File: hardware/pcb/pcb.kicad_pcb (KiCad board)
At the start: 2 copper layers, 5 parts, among them J1 PRT-12639, K1 KEYSW, U1 RP2040_Zero, U2 Nice_Nano_V2

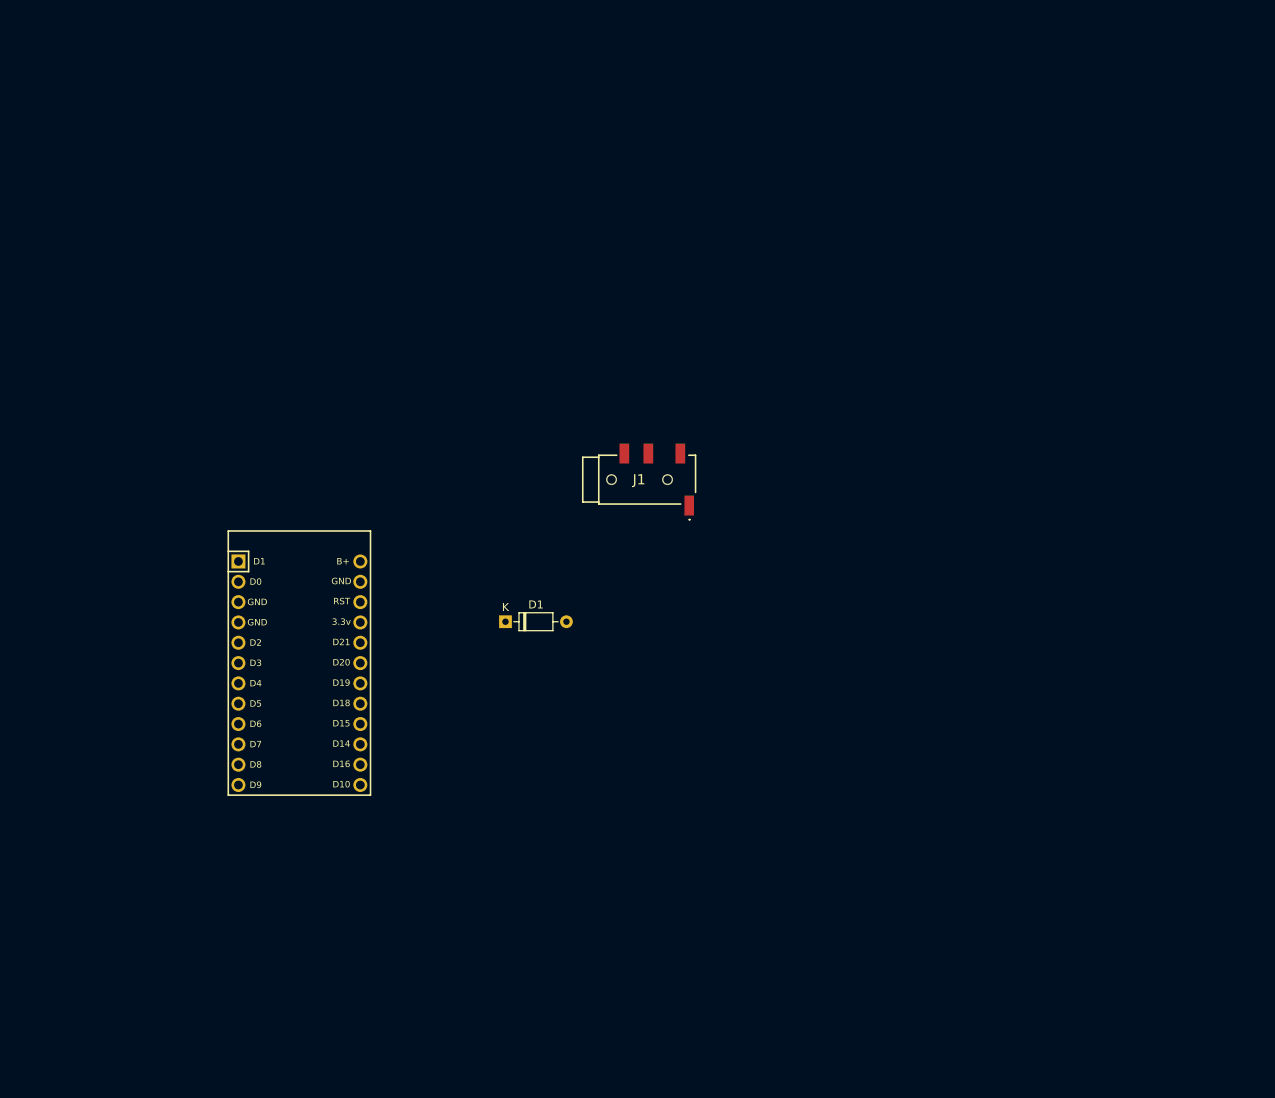
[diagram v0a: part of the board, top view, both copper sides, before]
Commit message: added 6X8 matrix and global labels
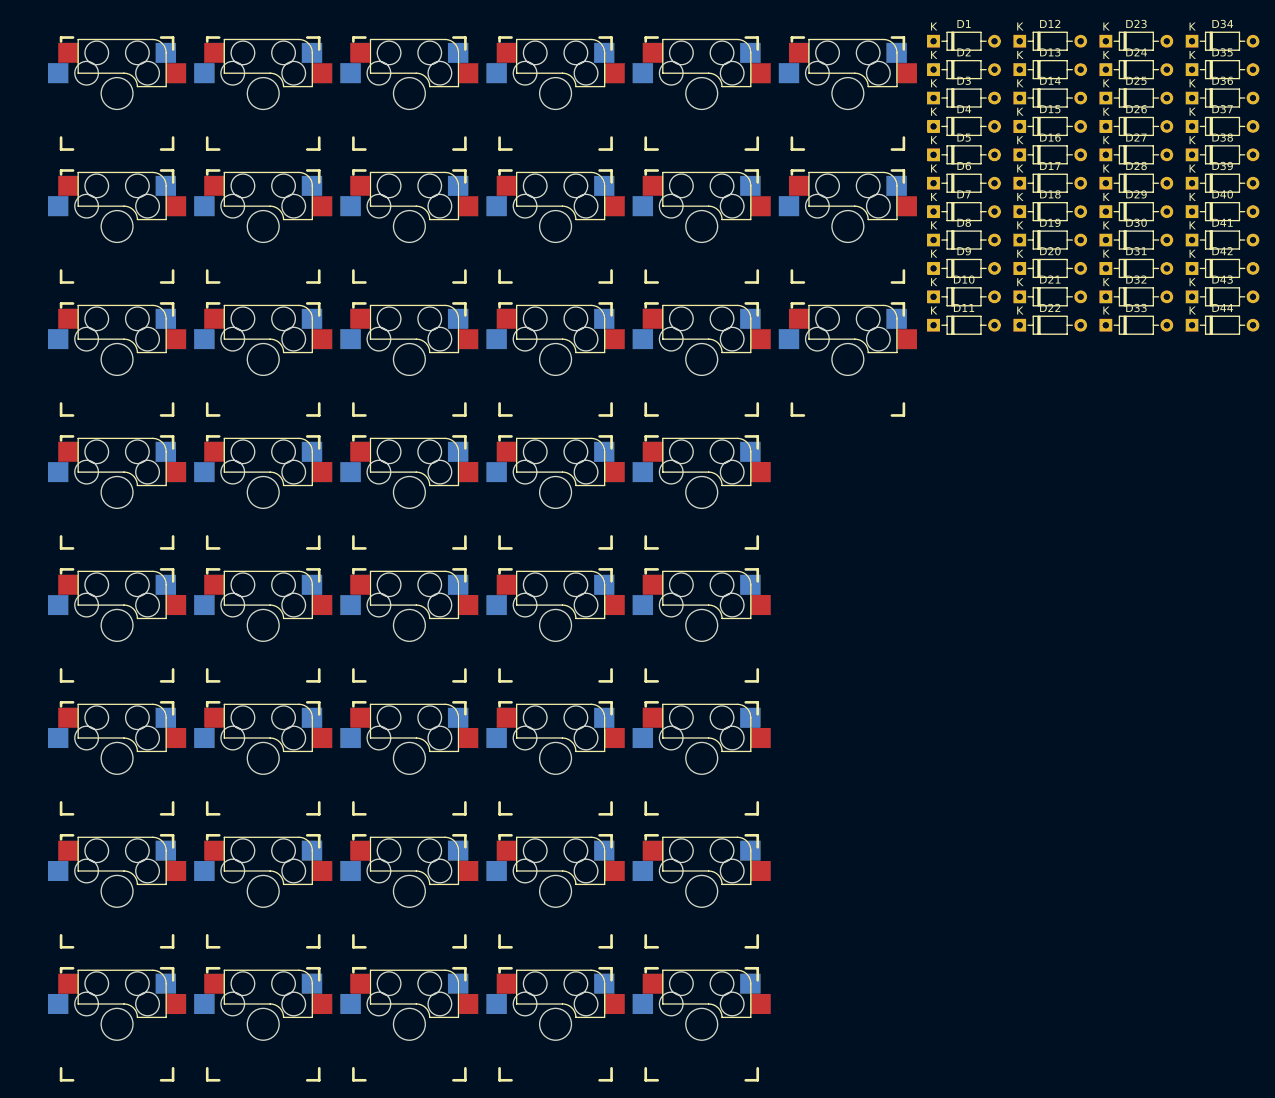
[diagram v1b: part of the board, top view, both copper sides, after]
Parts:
- removed J1: PRT-12639, foot:PRT12639
- removed U2: Nice_Nano_V2, ScottoKeebs_MCU:Nice_Nano_V2
- added D10: Diode, ScottoKeebs_Components:Diode_DO-35, F.Cu at (230.7, 56.4)
- added D11: Diode, ScottoKeebs_Components:Diode_DO-35, F.Cu at (230.7, 59.9)
- added D12: Diode, ScottoKeebs_Components:Diode_DO-35, F.Cu at (241.5, 24.4)
- added D13: Diode, ScottoKeebs_Components:Diode_DO-35, F.Cu at (241.5, 27.9)
- added D14: Diode, ScottoKeebs_Components:Diode_DO-35, F.Cu at (241.5, 31.5)
- added D15: Diode, ScottoKeebs_Components:Diode_DO-35, F.Cu at (241.5, 35.0)
- added D16: Diode, ScottoKeebs_Components:Diode_DO-35, F.Cu at (241.5, 38.6)
- added D17: Diode, ScottoKeebs_Components:Diode_DO-35, F.Cu at (241.5, 42.1)
- added D18: Diode, ScottoKeebs_Components:Diode_DO-35, F.Cu at (241.5, 45.7)
- added D19: Diode, ScottoKeebs_Components:Diode_DO-35, F.Cu at (241.5, 49.2)
- added D2: Diode, ScottoKeebs_Components:Diode_DO-35, F.Cu at (230.7, 27.9)
- added D20: Diode, ScottoKeebs_Components:Diode_DO-35, F.Cu at (241.5, 52.8)
- added D21: Diode, ScottoKeebs_Components:Diode_DO-35, F.Cu at (241.5, 56.4)
- added D22: Diode, ScottoKeebs_Components:Diode_DO-35, F.Cu at (241.5, 59.9)
- added D23: Diode, ScottoKeebs_Components:Diode_DO-35, F.Cu at (252.2, 24.4)
- added D24: Diode, ScottoKeebs_Components:Diode_DO-35, F.Cu at (252.2, 27.9)
- added D25: Diode, ScottoKeebs_Components:Diode_DO-35, F.Cu at (252.2, 31.5)
- added D26: Diode, ScottoKeebs_Components:Diode_DO-35, F.Cu at (252.2, 35.0)
- added D27: Diode, ScottoKeebs_Components:Diode_DO-35, F.Cu at (252.2, 38.6)
- added D28: Diode, ScottoKeebs_Components:Diode_DO-35, F.Cu at (252.2, 42.1)
- added D29: Diode, ScottoKeebs_Components:Diode_DO-35, F.Cu at (252.2, 45.7)
- added D3: Diode, ScottoKeebs_Components:Diode_DO-35, F.Cu at (230.7, 31.5)
- added D30: Diode, ScottoKeebs_Components:Diode_DO-35, F.Cu at (252.2, 49.2)
- added D31: Diode, ScottoKeebs_Components:Diode_DO-35, F.Cu at (252.2, 52.8)
- added D32: Diode, ScottoKeebs_Components:Diode_DO-35, F.Cu at (252.2, 56.4)
- added D33: Diode, ScottoKeebs_Components:Diode_DO-35, F.Cu at (252.2, 59.9)
- added D34: Diode, ScottoKeebs_Components:Diode_DO-35, F.Cu at (263.0, 24.4)
- added D35: Diode, ScottoKeebs_Components:Diode_DO-35, F.Cu at (263.0, 27.9)
- added D36: Diode, ScottoKeebs_Components:Diode_DO-35, F.Cu at (263.0, 31.5)
- added D37: Diode, ScottoKeebs_Components:Diode_DO-35, F.Cu at (263.0, 35.0)
- added D38: Diode, ScottoKeebs_Components:Diode_DO-35, F.Cu at (263.0, 38.6)
- added D39: Diode, ScottoKeebs_Components:Diode_DO-35, F.Cu at (263.0, 42.1)
- added D4: Diode, ScottoKeebs_Components:Diode_DO-35, F.Cu at (230.7, 35.0)
- added D40: Diode, ScottoKeebs_Components:Diode_DO-35, F.Cu at (263.0, 45.7)
- added D41: Diode, ScottoKeebs_Components:Diode_DO-35, F.Cu at (263.0, 49.2)
- added D42: Diode, ScottoKeebs_Components:Diode_DO-35, F.Cu at (263.0, 52.8)
- added D43: Diode, ScottoKeebs_Components:Diode_DO-35, F.Cu at (263.0, 56.4)
- added D44: Diode, ScottoKeebs_Components:Diode_DO-35, F.Cu at (263.0, 59.9)
- added D5: Diode, ScottoKeebs_Components:Diode_DO-35, F.Cu at (230.7, 38.6)
- added D6: Diode, ScottoKeebs_Components:Diode_DO-35, F.Cu at (230.7, 42.1)
- added D7: Diode, ScottoKeebs_Components:Diode_DO-35, F.Cu at (230.7, 45.7)
- added D8: Diode, ScottoKeebs_Components:Diode_DO-35, F.Cu at (230.7, 49.2)
- added D9: Diode, ScottoKeebs_Components:Diode_DO-35, F.Cu at (230.7, 52.8)
- added K10: KEYSW, vbdox:Kailh_MX_Socket_reversible, F.Cu at (146.9, 30.9)
- added K11: KEYSW, vbdox:Kailh_MX_Socket_reversible, F.Cu at (146.9, 47.6)
- added K12: KEYSW, vbdox:Kailh_MX_Socket_reversible, F.Cu at (146.9, 64.2)
- added K13: KEYSW, vbdox:Kailh_MX_Socket_reversible, F.Cu at (146.9, 80.8)
- added K14: KEYSW, vbdox:Kailh_MX_Socket_reversible, F.Cu at (146.9, 97.4)
- added K15: KEYSW, vbdox:Kailh_MX_Socket_reversible, F.Cu at (146.9, 114.0)
- added K16: KEYSW, vbdox:Kailh_MX_Socket_reversible, F.Cu at (146.9, 130.7)
- added K17: KEYSW, vbdox:Kailh_MX_Socket_reversible, F.Cu at (146.9, 147.3)
- added K18: KEYSW, vbdox:Kailh_MX_Socket_reversible, F.Cu at (165.2, 30.9)
- added K19: KEYSW, vbdox:Kailh_MX_Socket_reversible, F.Cu at (165.2, 47.6)
- added K2: KEYSW, vbdox:Kailh_MX_Socket_reversible, F.Cu at (128.6, 30.9)
- added K20: KEYSW, vbdox:Kailh_MX_Socket_reversible, F.Cu at (165.2, 64.2)
- added K21: KEYSW, vbdox:Kailh_MX_Socket_reversible, F.Cu at (165.2, 80.8)
- added K22: KEYSW, vbdox:Kailh_MX_Socket_reversible, F.Cu at (165.2, 97.4)
- added K23: KEYSW, vbdox:Kailh_MX_Socket_reversible, F.Cu at (165.2, 114.0)
- added K24: KEYSW, vbdox:Kailh_MX_Socket_reversible, F.Cu at (165.2, 130.7)
- added K25: KEYSW, vbdox:Kailh_MX_Socket_reversible, F.Cu at (165.2, 147.3)
- added K26: KEYSW, vbdox:Kailh_MX_Socket_reversible, F.Cu at (183.4, 30.9)
- added K27: KEYSW, vbdox:Kailh_MX_Socket_reversible, F.Cu at (183.4, 47.6)
- added K28: KEYSW, vbdox:Kailh_MX_Socket_reversible, F.Cu at (183.4, 64.2)
- added K29: KEYSW, vbdox:Kailh_MX_Socket_reversible, F.Cu at (183.4, 80.8)
- added K3: KEYSW, vbdox:Kailh_MX_Socket_reversible, F.Cu at (128.6, 47.6)
- added K30: KEYSW, vbdox:Kailh_MX_Socket_reversible, F.Cu at (183.4, 97.4)
- added K31: KEYSW, vbdox:Kailh_MX_Socket_reversible, F.Cu at (183.4, 114.0)
- added K32: KEYSW, vbdox:Kailh_MX_Socket_reversible, F.Cu at (183.4, 130.7)
- added K33: KEYSW, vbdox:Kailh_MX_Socket_reversible, F.Cu at (183.4, 147.3)
- added K34: KEYSW, vbdox:Kailh_MX_Socket_reversible, F.Cu at (201.7, 30.9)
- added K35: KEYSW, vbdox:Kailh_MX_Socket_reversible, F.Cu at (201.7, 47.6)
- added K36: KEYSW, vbdox:Kailh_MX_Socket_reversible, F.Cu at (201.7, 64.2)
- added K37: KEYSW, vbdox:Kailh_MX_Socket_reversible, F.Cu at (201.7, 80.8)
- added K38: KEYSW, vbdox:Kailh_MX_Socket_reversible, F.Cu at (201.7, 97.4)
- added K39: KEYSW, vbdox:Kailh_MX_Socket_reversible, F.Cu at (201.7, 114.0)
- added K4: KEYSW, vbdox:Kailh_MX_Socket_reversible, F.Cu at (128.6, 64.2)
- added K40: KEYSW, vbdox:Kailh_MX_Socket_reversible, F.Cu at (201.7, 130.7)
- added K41: KEYSW, vbdox:Kailh_MX_Socket_reversible, F.Cu at (201.7, 147.3)
- added K42: KEYSW, vbdox:Kailh_MX_Socket_reversible, F.Cu at (220.0, 30.9)
- added K43: KEYSW, vbdox:Kailh_MX_Socket_reversible, F.Cu at (220.0, 47.6)
- added K44: KEYSW, vbdox:Kailh_MX_Socket_reversible, F.Cu at (220.0, 64.2)
- added K5: KEYSW, vbdox:Kailh_MX_Socket_reversible, F.Cu at (128.6, 80.8)
- added K6: KEYSW, vbdox:Kailh_MX_Socket_reversible, F.Cu at (128.6, 97.4)
- added K7: KEYSW, vbdox:Kailh_MX_Socket_reversible, F.Cu at (128.6, 114.0)
- added K8: KEYSW, vbdox:Kailh_MX_Socket_reversible, F.Cu at (128.6, 130.7)
- added K9: KEYSW, vbdox:Kailh_MX_Socket_reversible, F.Cu at (128.6, 147.3)
- moved D1 90.2 mm to (230.7, 24.4)
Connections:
- D1 pad 2: unconnected-(D1-A-Pad2) -> Net-(D1-A)
- K1 pad 1: unconnected-(K1-Pad1) -> Net-(D1-A)

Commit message: schema init
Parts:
- added J1: PRT-12639, vbdox:PRT12639, B.Cu at (115.3, 24.9)
- added R1: 2.2K, ScottoKeebs_Components:Diode_DO-35, F.Cu at (95.7, 29.0)
- added R2: 2.2K, ScottoKeebs_Components:Diode_DO-35, F.Cu at (95.7, 34.4)
- D1, D10, D11, D12, D13, D14, D15, D16, D17, D18, D19, D2, D20, D21, D22, D23, D24, D25, D26, D27, D28, D29, D3, D30, D31, D32, D33, D34, D35, D36, D37, D38, D39, D4, D40, D41, D42, D43, D44, D5, D6, D7, D8, D9, U1: moved to B.Cu
- moved D37 211.7 mm to (84.6, 149.1), turned to 90 degrees
- moved D38 193.9 mm to (103.7, 149.1), turned to 90 degrees
- moved D26 188.4 mm to (79.9, 111.1), turned to 90 degrees
- moved D33 186.1 mm to (79.9, 130.2), turned to 90 degrees
- moved D35 182.3 mm to (122.7, 144.4), turned to 90 degrees
- moved D34 168.9 mm to (141.8, 142.0), turned to 90 degrees
- moved D12 168.7 mm to (79.9, 72.9), turned to 90 degrees
- moved D25 168.5 mm to (103.7, 111.0), turned to 90 degrees
- moved D20 166.3 mm to (79.9, 92.1), turned to 90 degrees
- moved D32 165.8 mm to (103.7, 130.1), turned to 90 degrees
- moved D36 152.2 mm to (160.8, 144.4), turned to 90 degrees
- moved D29 152.0 mm to (122.7, 125.3), turned to 90 degrees
- moved D13 144.9 mm to (103.7, 72.9), turned to 90 degrees
- moved D19 144.2 mm to (103.7, 92.0), turned to 90 degrees
- moved K37 138.5 mm to (79.6, 146.1)
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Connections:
- D1 pad 1: unconnected-(D1-K-Pad1) -> C0
- D10 pad 1: unconnected-(D10-K-Pad1) -> C3
- D11 pad 1: unconnected-(D11-K-Pad1) -> C4
- D12 pad 1: unconnected-(D12-K-Pad1) -> C5
- D13 pad 1: unconnected-(D13-K-Pad1) -> C6
- D14 pad 1: unconnected-(D14-K-Pad1) -> C0
- D15 pad 1: unconnected-(D15-K-Pad1) -> C1
- D16 pad 1: unconnected-(D16-K-Pad1) -> C2
- D17 pad 1: unconnected-(D17-K-Pad1) -> C3
- D18 pad 1: unconnected-(D18-K-Pad1) -> C4
- D19 pad 1: unconnected-(D19-K-Pad1) -> C5
- D2 pad 1: unconnected-(D2-K-Pad1) -> C1
- D20 pad 1: unconnected-(D20-K-Pad1) -> C6
- D21 pad 1: unconnected-(D21-K-Pad1) -> C0
- D22 pad 1: unconnected-(D22-K-Pad1) -> C1
- D23 pad 1: unconnected-(D23-K-Pad1) -> C2
- D24 pad 1: unconnected-(D24-K-Pad1) -> C3
- D25 pad 1: unconnected-(D25-K-Pad1) -> C4
- D26 pad 1: unconnected-(D26-K-Pad1) -> C5
- D27 pad 1: unconnected-(D27-K-Pad1) -> C6
- D28 pad 1: unconnected-(D28-K-Pad1) -> C7
- D29 pad 1: unconnected-(D29-K-Pad1) -> C0
- D3 pad 1: unconnected-(D3-K-Pad1) -> C2
- D30 pad 1: unconnected-(D30-K-Pad1) -> C1
- D31 pad 1: unconnected-(D31-K-Pad1) -> C2
- D32 pad 1: unconnected-(D32-K-Pad1) -> C3
- D33 pad 1: unconnected-(D33-K-Pad1) -> C4
- D34 pad 1: unconnected-(D34-K-Pad1) -> C5
- D35 pad 1: unconnected-(D35-K-Pad1) -> C6
- D36 pad 1: unconnected-(D36-K-Pad1) -> C7
- D37 pad 1: unconnected-(D37-K-Pad1) -> C0
- D38 pad 1: unconnected-(D38-K-Pad1) -> C1
- D39 pad 1: unconnected-(D39-K-Pad1) -> C2
- D4 pad 1: unconnected-(D4-K-Pad1) -> C3
- D40 pad 1: unconnected-(D40-K-Pad1) -> C3
- D41 pad 1: unconnected-(D41-K-Pad1) -> C4
- D42 pad 1: unconnected-(D42-K-Pad1) -> C5
- D43 pad 1: unconnected-(D43-K-Pad1) -> C6
- D44 pad 1: unconnected-(D44-K-Pad1) -> C7
- D5 pad 1: unconnected-(D5-K-Pad1) -> C4
- D6 pad 1: unconnected-(D6-K-Pad1) -> C5
- D7 pad 1: unconnected-(D7-K-Pad1) -> C0
- D8 pad 1: unconnected-(D8-K-Pad1) -> C1
- D9 pad 1: unconnected-(D9-K-Pad1) -> C2
- K1 pad 2: unconnected-(K1-Pad2) -> R0
- K10 pad 2: unconnected-(K10-Pad2) -> R1
- K11 pad 2: unconnected-(K11-Pad2) -> R1
- K12 pad 2: unconnected-(K12-Pad2) -> R1
- K13 pad 2: unconnected-(K13-Pad2) -> R1
- K14 pad 2: unconnected-(K14-Pad2) -> R2
- K15 pad 2: unconnected-(K15-Pad2) -> R2
- K16 pad 2: unconnected-(K16-Pad2) -> R2
- K17 pad 2: unconnected-(K17-Pad2) -> R2
- K18 pad 2: unconnected-(K18-Pad2) -> R2
- K19 pad 2: unconnected-(K19-Pad2) -> R2
- K2 pad 2: unconnected-(K2-Pad2) -> R0
- K20 pad 2: unconnected-(K20-Pad2) -> R2
- K21 pad 2: unconnected-(K21-Pad2) -> R3
- K22 pad 2: unconnected-(K22-Pad2) -> R3
- K23 pad 2: unconnected-(K23-Pad2) -> R3
- K24 pad 2: unconnected-(K24-Pad2) -> R3
- K25 pad 2: unconnected-(K25-Pad2) -> R3
- K26 pad 2: unconnected-(K26-Pad2) -> R3
- K27 pad 2: unconnected-(K27-Pad2) -> R3
- K28 pad 2: unconnected-(K28-Pad2) -> R3
- K29 pad 2: unconnected-(K29-Pad2) -> R4
- K3 pad 2: unconnected-(K3-Pad2) -> R0
- K30 pad 2: unconnected-(K30-Pad2) -> R4
- K31 pad 2: unconnected-(K31-Pad2) -> R4
- K32 pad 2: unconnected-(K32-Pad2) -> R4
- K33 pad 2: unconnected-(K33-Pad2) -> R4
- K34 pad 2: unconnected-(K34-Pad2) -> R4
- K35 pad 2: unconnected-(K35-Pad2) -> R4
- K36 pad 2: unconnected-(K36-Pad2) -> R4
- K37 pad 2: unconnected-(K37-Pad2) -> R5
- K38 pad 2: unconnected-(K38-Pad2) -> R5
- K39 pad 2: unconnected-(K39-Pad2) -> R5
- K4 pad 2: unconnected-(K4-Pad2) -> R0
- K40 pad 2: unconnected-(K40-Pad2) -> R5
- K41 pad 2: unconnected-(K41-Pad2) -> R5
- K42 pad 2: unconnected-(K42-Pad2) -> R5
- K43 pad 2: unconnected-(K43-Pad2) -> R5
- K44 pad 2: unconnected-(K44-Pad2) -> R5
- K5 pad 2: unconnected-(K5-Pad2) -> R0
- K6 pad 2: unconnected-(K6-Pad2) -> R0
- K7 pad 2: unconnected-(K7-Pad2) -> R1
- K8 pad 2: unconnected-(K8-Pad2) -> R1
- K9 pad 2: unconnected-(K9-Pad2) -> R1
- U1 pad 1: unconnected-(U1-0-Pad1) -> C0
- U1 pad 13: unconnected-(U1-12-Pad13) -> SDA
- U1 pad 14: unconnected-(U1-13-Pad14) -> SCL
- U1 pad 15: unconnected-(U1-14-Pad15) -> R5
- U1 pad 16: unconnected-(U1-15-Pad16) -> R4
- U1 pad 17: unconnected-(U1-26-Pad17) -> R3
- U1 pad 18: unconnected-(U1-27-Pad18) -> R2
- U1 pad 19: unconnected-(U1-28-Pad19) -> R1
- U1 pad 2: unconnected-(U1-1-Pad2) -> C1
- U1 pad 20: unconnected-(U1-29-Pad20) -> R0
- U1 pad 22: unconnected-(U1-GND-Pad22) -> GND
- U1 pad 23: unconnected-(U1-5V-Pad23) -> VCC
- U1 pad 3: unconnected-(U1-2-Pad3) -> C2
- U1 pad 4: unconnected-(U1-3-Pad4) -> C3
- U1 pad 5: unconnected-(U1-4-Pad5) -> C4
- U1 pad 6: unconnected-(U1-5-Pad6) -> C5
- U1 pad 7: unconnected-(U1-6-Pad7) -> C6
- U1 pad 8: unconnected-(U1-7-Pad8) -> C7
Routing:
- net Net-(D42-A): track 0.00 -> 3.13 mm
- net Net-(D41-A): track 0.00 -> 3.13 mm
- net Net-(D44-A): track 0.00 -> 3.13 mm
- net Net-(D43-A): track 0.00 -> 3.13 mm
- net Net-(D40-A): track 0.00 -> 3.13 mm
- net Net-(D39-A): track 0.00 -> 3.13 mm
- net Net-(D36-A): track 0.00 -> 3.13 mm
- net Net-(D23-A): track 0.00 -> 3.13 mm
- net Net-(D32-A): track 0.00 -> 3.13 mm
- net Net-(D20-A): track 0.00 -> 3.13 mm
- net Net-(D35-A): track 0.00 -> 3.13 mm
- net Net-(D34-A): track 0.00 -> 3.13 mm
- net Net-(D22-A): track 0.00 -> 3.13 mm
- net Net-(D18-A): track 0.00 -> 3.13 mm
- net Net-(D6-A): track 0.00 -> 3.13 mm
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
